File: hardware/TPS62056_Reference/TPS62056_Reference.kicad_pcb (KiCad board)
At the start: 2 copper layers, 3 parts, among them J1 CONN_6, U1 TPS6205X

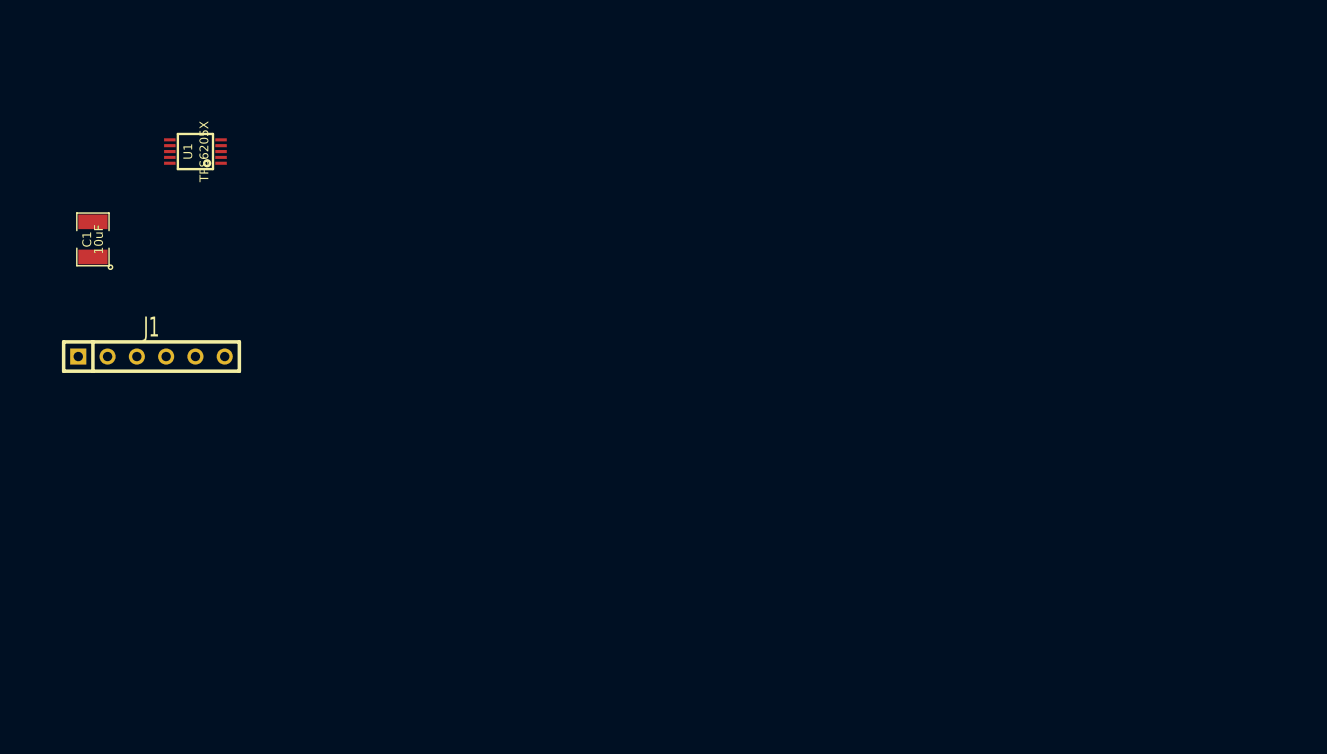
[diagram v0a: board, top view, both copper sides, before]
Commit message: Found parts, created footprints, added to board.
Board had all footprints on it, but it completely rat's nest.
Spreadsheet BOM created, but not yet in repo.
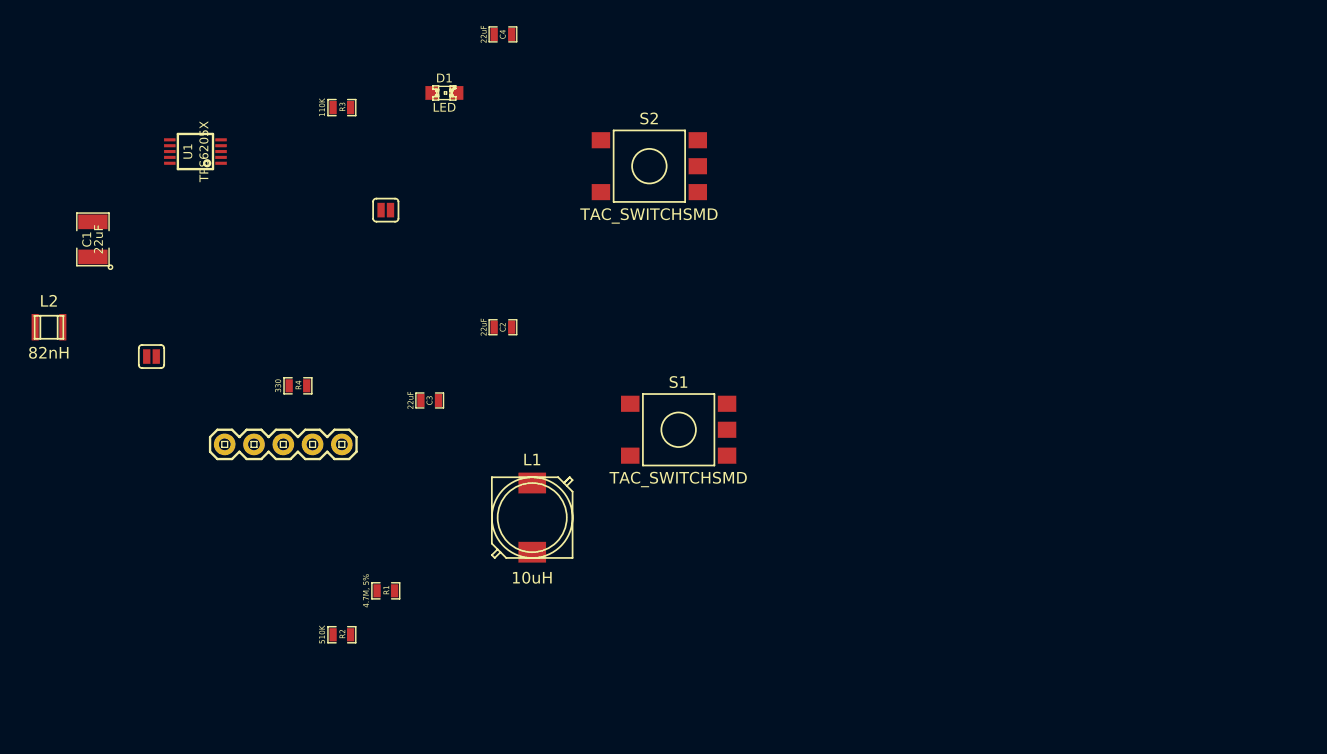
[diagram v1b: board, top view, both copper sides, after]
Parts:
- added C2: 22uF, SM0603_Capa, F.Cu at (63.5, 44.5)
- added C3: 22uF, SM0603_Capa, F.Cu at (57.1, 50.8)
- added C4: 22uF, SM0603_Capa, F.Cu at (63.5, 19.1)
- added D1: LED, LED-0805, F.Cu at (58.4, 24.1)
- added J2: GS2, SparkFun-SJ_2S, F.Cu at (53.3, 34.3)
- added L1: 10uH, Bourns_SRR7032, F.Cu at (66.0, 61.0)
- added L2: 82nH, Bourns_PM1008, F.Cu at (24.1, 44.5)
- added P1: CONN_5, SparkFun-1X05, F.Cu at (39.4, 54.6)
- added R1: 4.7M, 5%, SM0603_Resistor, F.Cu at (53.3, 67.3)
- added R2: 510K, SM0603_Resistor, F.Cu at (49.5, 71.1)
- added R3: 110K, SM0603_Resistor, F.Cu at (49.5, 25.4)
- added R4: 330, SM0603_Resistor, F.Cu at (45.7, 49.5)
- added S1: TAC_SWITCHSMD, Alps_TACT_SKHM_Series, F.Cu at (78.7, 53.3)
- added S2: TAC_SWITCHSMD, Alps_TACT_SKHM_Series, F.Cu at (76.2, 30.5)
- C1: value 10uF -> 22uF
- J1: value CONN_6 -> GS2; footprint SIL-6 -> SparkFun-SJ_2S
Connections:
- C1 pad 1: /VIN -> +BATT
- C1 pad 2: (no net) -> GND
- J1 pad 1: /EN -> +BATT
- J1 pad 2: /VIN -> /EN
- U1 pad 1: /VIN -> +BATT
- U1 pad 10: (no net) -> GND
- U1 pad 3: (no net) -> GND
- U1 pad 4: /PG -> GND
- U1 pad 5: (no net) -> /FB
- U1 pad 6: (no net) -> /LBI
- U1 pad 7: (no net) -> GND
- U1 pad 9: N-0000013 -> /SW

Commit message: Board is almost completely routed
Except for an error that prevents me from connecting anything to the
IC...
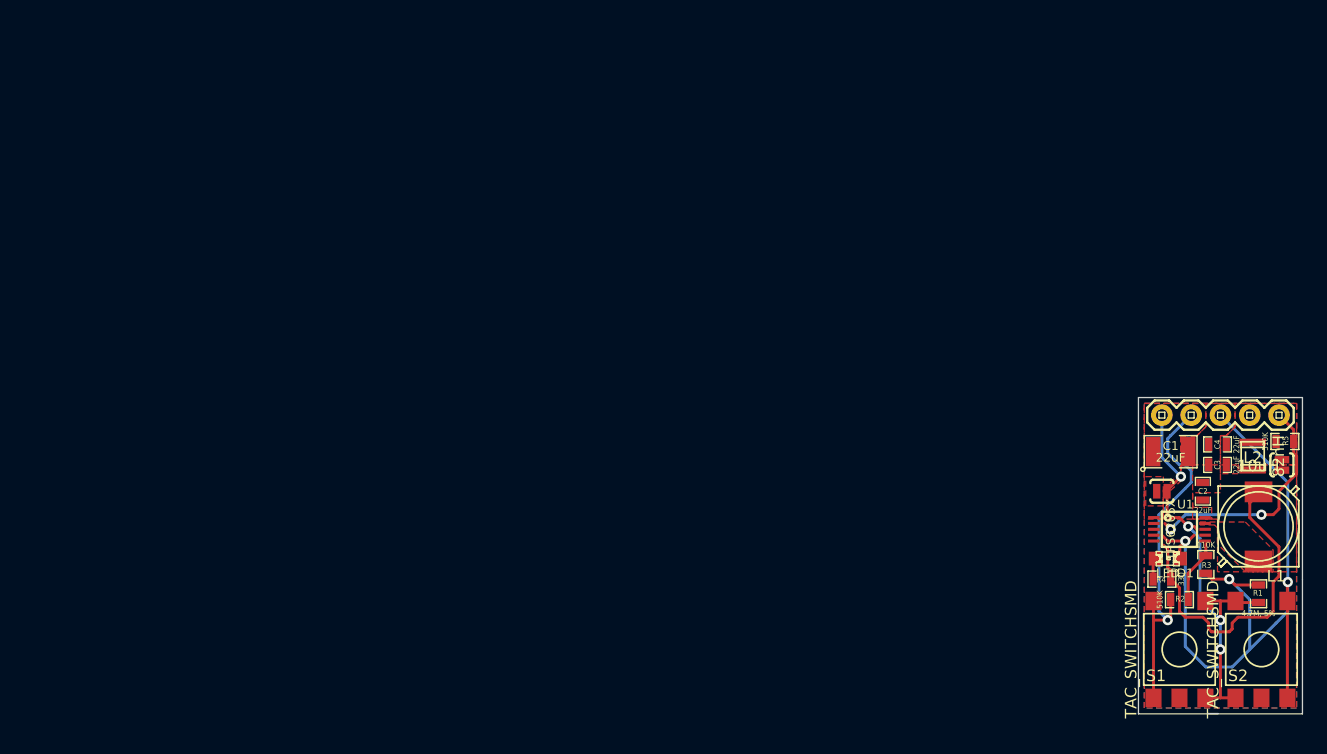
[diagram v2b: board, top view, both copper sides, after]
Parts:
- added R5: 510K, SM0603_Resistor, F.Cu at (131.3, 54.4)
- J1, J2: footprint SparkFun-SJ_2S -> SparkFun-SJ_2S-NO
- moved L2 105.0 mm to (128.5, 55.6), turned to 90 degrees
- moved C1 95.3 mm to (121.4, 55.2), turned to 0 degrees
- moved U1 91.4 mm to (122.2, 62.0), turned to 270 degrees
- moved J1 88.4 mm to (120.7, 58.7)
- moved R3 84.8 mm to (124.5, 65.0), turned to 270 degrees
- moved P1 81.3 mm to (120.7, 52.1)
- moved J2 80.8 mm to (131.1, 56.4), turned to 90 degrees
- moved R4 76.8 mm to (120.7, 66.3), turned to 180 degrees
- moved R1 75.7 mm to (129.0, 67.6), turned to 90 degrees
- moved D1 74.6 mm to (121.2, 64.5)
- moved R2 72.7 mm to (122.2, 68.1)
- moved C4 71.5 mm to (125.5, 54.6), turned to 180 degrees
- moved C3 68.6 mm to (125.5, 56.4), turned to 180 degrees
- moved S2 67.6 mm to (129.3, 72.4), turned to 270 degrees
- moved L1 63.0 mm to (129.0, 61.7), turned to 180 degrees
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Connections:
- C4 pad 1: (no net) -> /VOUT
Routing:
- net GND: track 0.00 -> 67.0 mm, vias 0 -> 3
- net /EN: track 0.00 -> 37.9 mm, vias 0 -> 4
- net +BATT: track 0.00 -> 33.3 mm, vias 0 -> 1
- net /FB: track 0.00 -> 28.4 mm
- net /LBO: track 0.00 -> 20.2 mm, vias 0 -> 2
- net /LBI: track 0.00 -> 5.97 mm
- net N-000004: track 0.00 -> 1.87 mm
- added copper zone on F.Cu, net +BATT
- added copper zone on F.Cu, net /FB
- added copper zone on F.Cu, net /SW
- added copper zone on F.Cu, net /VOUT
- added copper zone on B.Cu, net GND
- added copper zone on F.Cu, net GND
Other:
- board outline added: 14.2 x 27.4 mm
- rule pad_to_mask_clearance: 0 -> 0.00254
- board text added: "EN"
- board text added: "GND"
- board text added: "LBO"
- board text added: "OFF"
- board text added: "ON"
- board text added: "VIN"
- board text added: "VOUT"

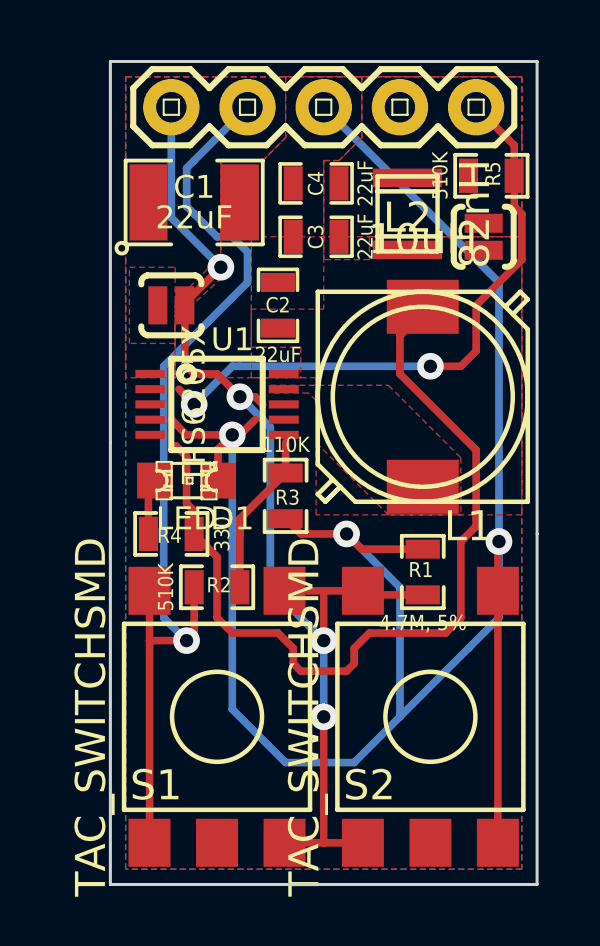
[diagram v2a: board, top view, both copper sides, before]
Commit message: Board completed
Added silkscreen help and connected the rest of the pins
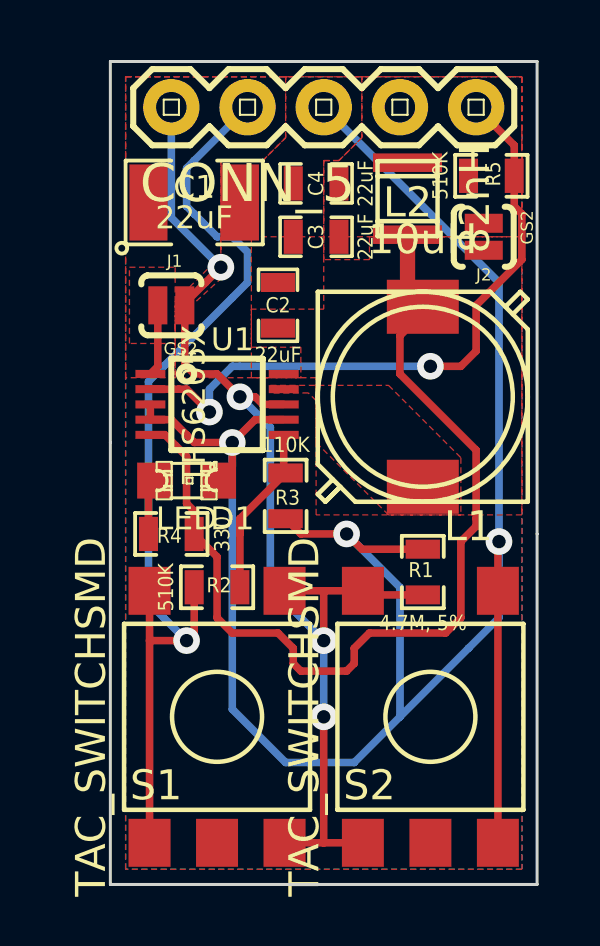
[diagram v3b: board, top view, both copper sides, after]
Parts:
- moved L2 0.51 mm to (128.5, 55.1)
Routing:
- net /FB: track 28.4 -> 32.1 mm
- net +BATT: track 33.3 -> 36.2 mm
- net GND: track 67.0 -> 68.9 mm
- net /LBO: track 20.2 -> 21.9 mm
- net /EN: track 37.9 -> 38.6 mm
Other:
- net class Default: clearance 0.254 -> 0.2032
- rule trace_clearance: 0.254 -> 0.2032
- rule via_min_drill: 0.508 -> 0.3302
- rule via_min_size: 0.889 -> 0.6858
- board text added: "Reference"
- board text added: "TPS62056"
- board text added: "v1.0"
- board text added: "→3.3-11V ←3.3V ←0.8A"

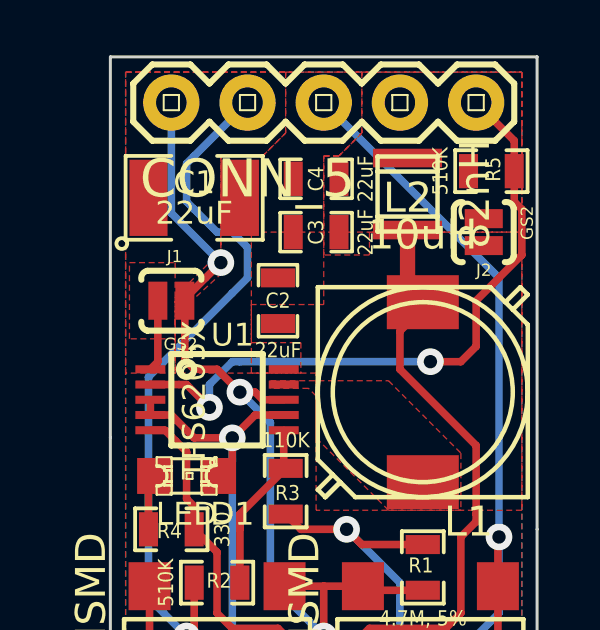
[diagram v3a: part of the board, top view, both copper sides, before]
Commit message: Added more via stitching and gerbers
More via stitching between front & back ground plane and adjusted planes
to fit vias.
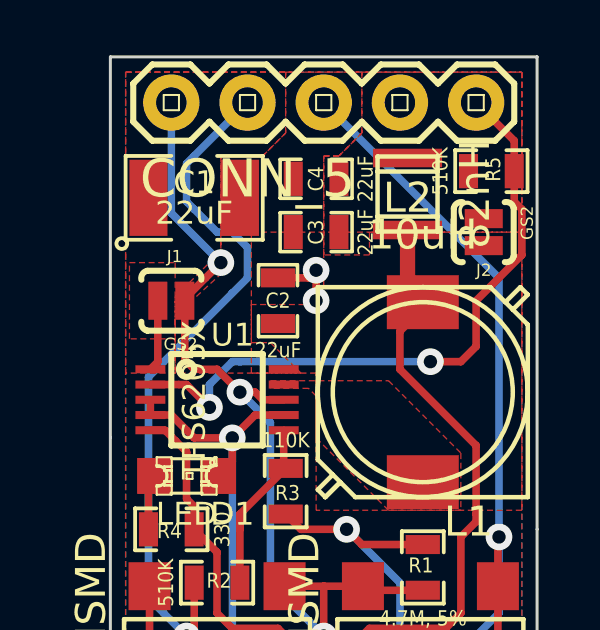
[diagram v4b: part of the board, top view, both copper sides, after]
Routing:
- net GND: track 68.9 -> 71.3 mm, vias 3 -> 5
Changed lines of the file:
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@@
     (thickness 1.6)
     (drawings 36)
-    (tracks 140)
+    (tracks 145)
     (zones 0)
     (modules 18)
@@
   (layers
     (15 F.Cu signal)
-    (0 B.Cu signal hide)
+    (0 B.Cu signal)
     (16 B.Adhes user hide)
     (17 F.Adhes user hide)
@@
   )
   (setup
-    (last_trace_width 0.508)
+    (last_trace_width 0.254)
     (user_trace_width 0.381)
     (user_trace_width 0.508)
@@
   (segment (start 132.08 54.356) (end 132.08 53.34) (width 0.254) (layer F.Cu) (net 5))
   (segment (start 132.08 53.34) (end 130.81 52.07) (width 0.254) (layer F.Cu) (net 5))
+  (segment (start 125.476 58.674) (end 125.476 57.658) (width 0.254) (layer F.Cu) (net 8))
+  (segment (start 125.222 57.912) (end 125.476 57.658) (width 0.254) (layer F.Cu) (net 8))
+  (via (at 125.476 57.658) (size 0.889) (layers F.Cu B.Cu) (net 8))
+  (segment (start 125.222 57.912) (end 124.206 57.912) (width 0.254) (layer F.Cu) (net 8))
+  (via (at 125.476 58.674) (size 0.889) (layers F.Cu B.Cu) (net 8))
   (segment (start 121.158 62.992) (end 121.412 63.246) (width 0.254) (layer F.Cu) (net 8))
   (segment (start 120.65 62.484) (end 121.158 62.992) (width 0.254) (layer F.Cu) (net 8))
@@
       (pts
         (xy 127 53.086) (xy 126.238 53.848) (xy 125.73 53.848) (xy 125.73 58.801) (xy 123.317 58.801)
-        (xy 123.317 60.071) (xy 124.968 60.071) (xy 124.968 61.087) (xy 120.777 61.087) (xy 120.777 59.182)
+        (xy 123.317 60.071) (xy 123.952 60.071) (xy 124.968 61.087) (xy 120.777 61.087) (xy 120.777 59.182)
         (xy 122.301 57.785) (xy 122.301 53.848) (xy 123.698 53.848) (xy 124.46 53.086) (xy 124.46 51.054)
         (xy 127 51.054)
